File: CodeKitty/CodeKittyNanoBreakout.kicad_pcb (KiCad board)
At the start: 2 copper layers, 17.8 x 43.2 mm, 11 parts, among them P1 CONN_01X02, P2 CONN_01X02, P3 CONN_01X03, P4 CONN_01X03, P5 CONN_01X02, U1 ArduinoNano

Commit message: update of codekitty
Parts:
- removed R3: R, Resistors_SMD:R_0805_HandSoldering
- added F1: F_Small, DM_Custom:DM_FUSE_PTC0ZCG, B.Cu at (201.5, 93.7)
- added SP1: SPEAKER, DM_Custom:DM_PiezSMD_PMKCS0909E4000-R1, B.Cu at (205.6, 114.3)
- added SW1: SW_PUSH_SMALL_H, DM_Custom:DM_SMD_BUTTON_PTS810, F.Cu at (203.7, 84.3)
- added SW2: Switch_SPDT_x2, DM_Custom:DM_SPDT_RTAngle_JS102011SAQN, B.Cu at (203.8, 84.5)
- R1: moved to F.Cu
- U1: moved to B.Cu
- moved G*** 25.0 mm to (205.4, 111.2)
- moved R2 20.3 mm to (209.5, 87.3), turned to 90 degrees
- moved P4 13.2 mm to (209.5, 105.7), turned to 0 degrees
- moved P2 10.5 mm to (205.6, 94.5), turned to 0 degrees
- moved R1 10.2 mm to (209.5, 87.3)
- moved P5 9.86 mm to (201.7, 105.7), turned to 0 degrees
- moved P3 6.37 mm to (205.7, 105.7), turned to 0 degrees
- moved D1 5.35 mm to (210.9, 83.7), turned to 180 degrees
- moved P1 4.17 mm to (209.6, 94.5), turned to 0 degrees
- moved U1 0.06 mm to (205.7, 104.1)
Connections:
- P1 pad 2: VCC -> Net-(P1-Pad2)
- P5 pad 2: Net-(P5-Pad2) -> BUZZ
- U1 pad 3: Net-(U1-Pad3) -> RST
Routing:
- net RST: track 0.00 -> 40.5 mm, vias 0 -> 2
- net GND: track 4.40 -> 26.9 mm, vias 0 -> 3
- net TAIL: track 24.4 -> 3.95 mm, vias 1 -> 0
- net VCC: track 12.0 -> 32.1 mm, vias 1 -> 2
- net 5V: track 52.5 -> 37.6 mm, vias 1 -> 0
- net RSERVO: track 5.23 -> 15.2 mm
- net BUZZ: track 22.5 -> 32.1 mm
- net Net-(P1-Pad2): track 0.00 -> 8.56 mm, vias 0 -> 1
- net Net-(F1-Pad1): track 0.00 -> 7.31 mm
- net Net-(D1-Pad1): track 9.52 -> 4.48 mm, vias 0 -> 1
- net LSERVO: track 5.50 -> 10.4 mm
- net Net-(P2-Pad2): track 3.88 -> 8.13 mm, vias 0 -> 2
- net Net-(P5-Pad2): track 4.04 -> 0.00 mm
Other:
- board text added: "CodeKitty DM100917"
- board text removed: "CodeKitty DM073117"

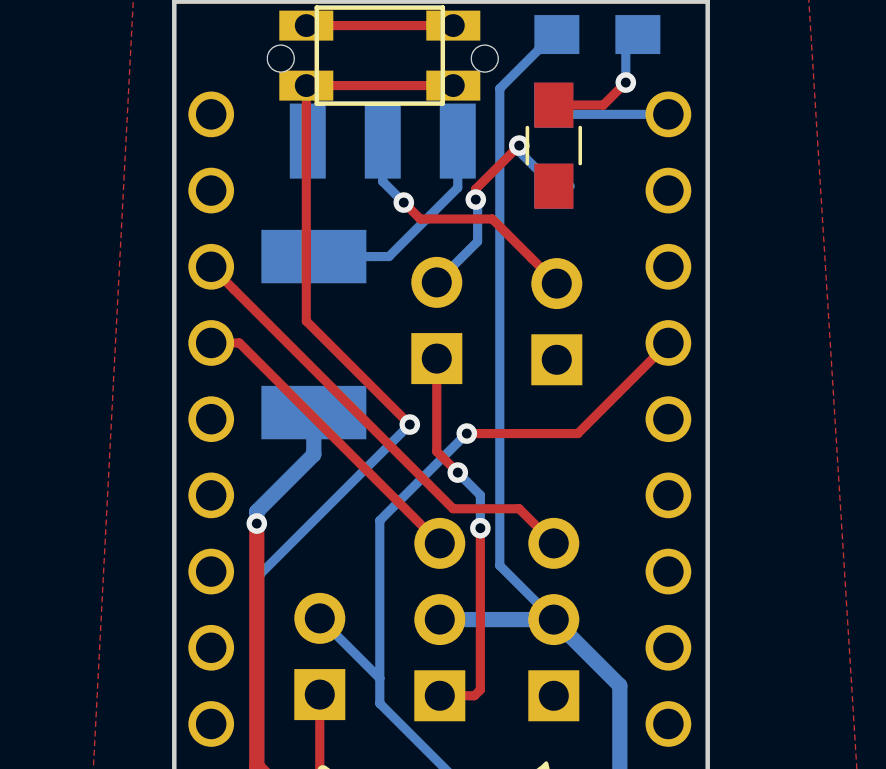
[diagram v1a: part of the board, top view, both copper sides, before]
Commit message: added fsilk letters for connectors for codeKitty
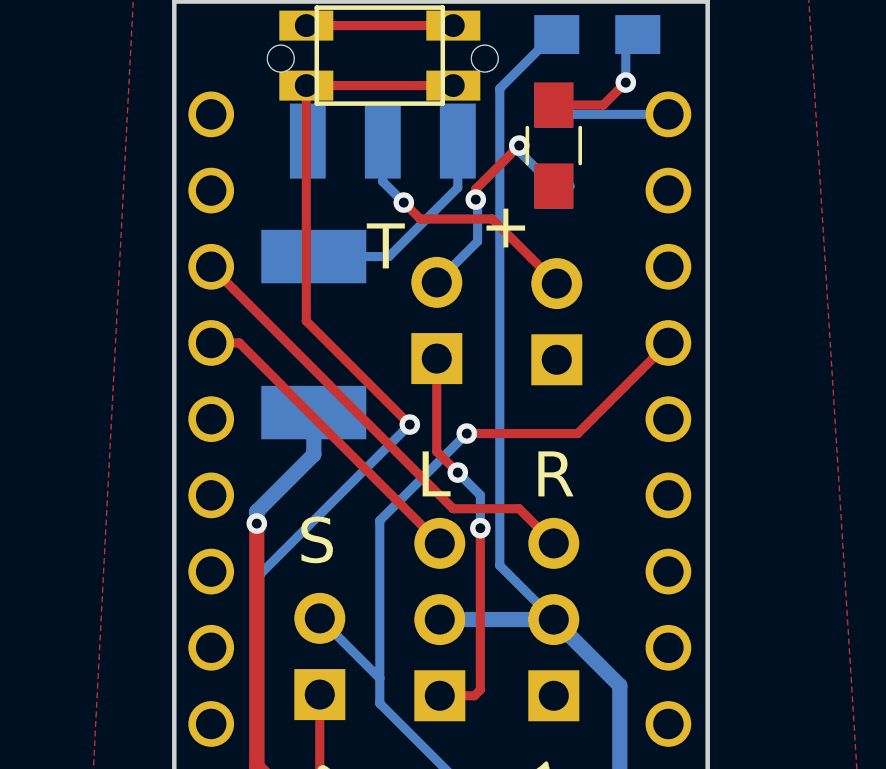
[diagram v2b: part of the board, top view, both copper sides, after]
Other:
- board text added: "+"
- board text added: "L"
- board text added: "R"
- board text added: "S"
- board text added: "T"
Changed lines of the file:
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@@
     (area 196.774999 82.474999 214.705001 125.805001)
     (thickness 1.6)
-    (drawings 16)
+    (drawings 21)
     (tracks 83)
     (zones 0)
@@
     (0 F.Cu signal)
     (31 B.Cu signal)
-    (32 B.Adhes user hide)
-    (33 F.Adhes user hide)
-    (34 B.Paste user hide)
-    (35 F.Paste user hide)
-    (36 B.SilkS user hide)
-    (37 F.SilkS user hide)
-    (38 B.Mask user hide)
+    (32 B.Adhes user)
+    (33 F.Adhes user)
+    (34 B.Paste user)
+    (35 F.Paste user)
+    (36 B.SilkS user)
+    (37 F.SilkS user)
+    (38 B.Mask user)
     (39 F.Mask user)
     (40 Dwgs.User user hide)
@@
     (42 Eco1.User user hide)
     (43 Eco2.User user hide)
-    (44 Edge.Cuts user hide)
+    (44 Edge.Cuts user)
     (45 Margin user hide)
     (46 B.CrtYd user hide)
@@
     (pad "" np_thru_hole circle (at 3.4 0) (size 0.9 0.9) (drill 0.9) (layers *.Cu *.Mask))
   )
+  (gr_text S (at 201.6 100.55) (layer F.SilkS)
+    (effects (font (size 1.5 1.5) (thickness 0.3)))
+  )
+  (gr_text L (at 205.5 98.35) (layer F.SilkS)
+    (effects (font (size 1.5 1.5) (thickness 0.3)))
+  )
+  (gr_text R (at 209.5 98.35) (layer F.SilkS)
+    (effects (font (size 1.5 1.5) (thickness 0.3)))
+  )
+  (gr_text T (at 203.9 90.75) (layer F.SilkS)
+    (effects (font (size 1.5 1.5) (thickness 0.3)))
+  )
+  (gr_text + (at 207.9 90.05) (layer F.SilkS)
+    (effects (font (size 1.5 1.5) (thickness 0.3)))
+  )
   (gr_text 1 (at 186.1 78.55) (layer B.SilkS)

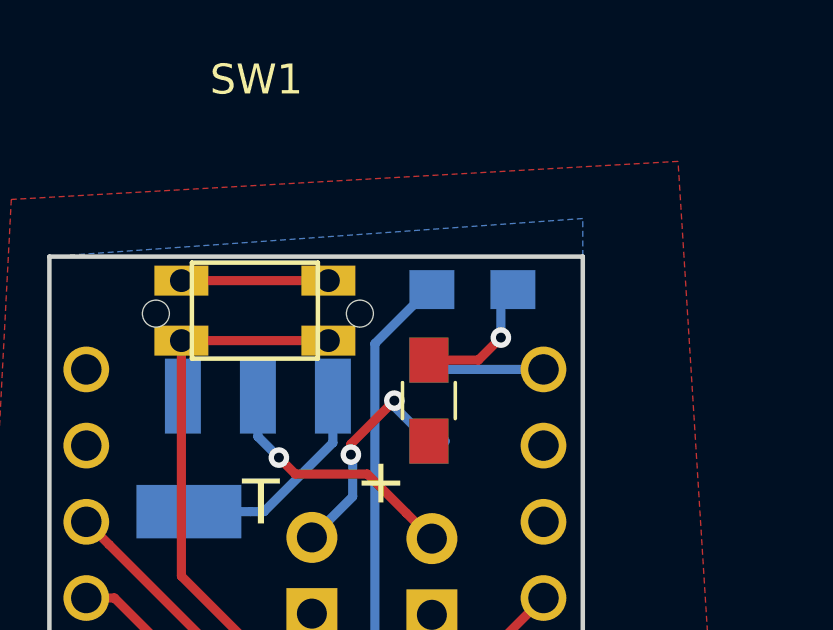
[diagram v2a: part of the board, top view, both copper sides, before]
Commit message: moved led to fside ck
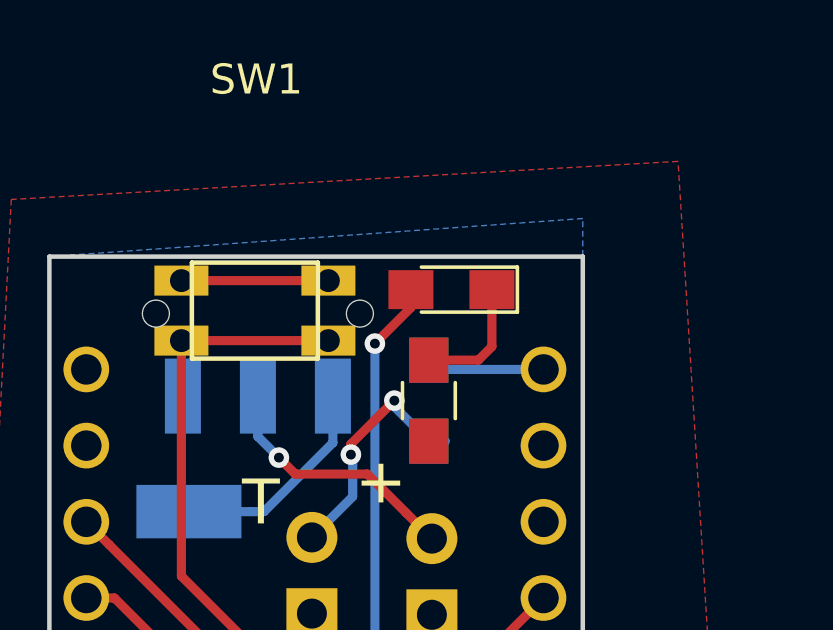
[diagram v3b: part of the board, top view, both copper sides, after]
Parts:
- D1: moved to F.Cu
- moved D1 0.70 mm to (210.2, 83.7)
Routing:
- net 5V: track 37.6 -> 37.2 mm, vias 0 -> 1
- net Net-(D1-Pad1): track 4.48 -> 4.19 mm, vias 1 -> 0
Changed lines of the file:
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@@
     (thickness 1.6)
     (drawings 21)
-    (tracks 83)
+    (tracks 82)
     (zones 0)
     (modules 14)
@@
     (add_net VCC)
   )
-  (module LEDs:LED_0805_HandSoldering (layer B.Cu)
-    (at 210.95 83.65 180)
+  (module LEDs:LED_0805_HandSoldering (layer F.Cu)
+    (at 210.25 83.65 180)
     (descr "Resistor SMD 0805, hand soldering")
     (tags "resistor 0805")
     (attr smd)
-    (fp_text reference D1 (at 0 1.7 180) (layer B.Fab)
-      (effects (font (size 1 1) (thickness 0.15)) (justify mirror))
-    )
-    (fp_text value LED (at 0 -1.75 180) (layer B.Fab)
-      (effects (font (size 1 1) (thickness 0.15)) (justify mirror))
-    )
-    (fp_line (start -0.4 0.4) (end -0.4 -0.4) (layer B.Fab) (width 0.1))
-    (fp_line (start -0.4 0) (end 0.2 0.4) (layer B.Fab) (width 0.1))
-    (fp_line (start 0.2 -0.4) (end -0.4 0) (layer B.Fab) (width 0.1))
-    (fp_line (start 0.2 0.4) (end 0.2 -0.4) (layer B.Fab) (width 0.1))
-    (fp_line (start -1 -0.62) (end -1 0.62) (layer B.Fab) (width 0.1))
-    (fp_line (start 1 -0.62) (end -1 -0.62) (layer B.Fab) (width 0.1))
-    (fp_line (start 1 0.62) (end 1 -0.62) (layer B.Fab) (width 0.1))
-    (fp_line (start -1 0.62) (end 1 0.62) (layer B.Fab) (width 0.1))
-    (fp_line (start 1 -0.75) (end -2.2 -0.75) (layer B.SilkS) (width 0.12))
-    (fp_line (start -2.2 0.75) (end 1 0.75) (layer B.SilkS) (width 0.12))
-    (fp_line (start -2.35 0.9) (end 2.35 0.9) (layer B.CrtYd) (width 0.05))
-    (fp_line (start -2.35 0.9) (end -2.35 -0.9) (layer B.CrtYd) (width 0.05))
-    (fp_line (start 2.35 -0.9) (end 2.35 0.9) (layer B.CrtYd) (width 0.05))
-    (fp_line (start 2.35 -0.9) (end -2.35 -0.9) (layer B.CrtYd) (width 0.05))
-    (fp_line (start -2.2 0.75) (end -2.2 -0.75) (layer B.SilkS) (width 0.12))
-    (pad 1 smd rect (at -1.35 0 180) (size 1.5 1.3) (layers B.Cu B.Paste B.Mask)
+    (fp_text reference D1 (at 0 -1.7 180) (layer F.Fab)
+      (effects (font (size 1 1) (thickness 0.15)))
+    )
+    (fp_text value LED (at 0 1.75 180) (layer F.Fab)
+      (effects (font (size 1 1) (thickness 0.15)))
+    )
+    (fp_line (start -0.4 -0.4) (end -0.4 0.4) (layer F.Fab) (width 0.1))
+    (fp_line (start -0.4 0) (end 0.2 -0.4) (layer F.Fab) (width 0.1))
+    (fp_line (start 0.2 0.4) (end -0.4 0) (layer F.Fab) (width 0.1))
+    (fp_line (start 0.2 -0.4) (end 0.2 0.4) (layer F.Fab) (width 0.1))
+    (fp_line (start -1 0.62) (end -1 -0.62) (layer F.Fab) (width 0.1))
+    (fp_line (start 1 0.62) (end -1 0.62) (layer F.Fab) (width 0.1))
+    (fp_line (start 1 -0.62) (end 1 0.62) (layer F.Fab) (width 0.1))
+    (fp_line (start -1 -0.62) (end 1 -0.62) (layer F.Fab) (width 0.1))
+    (fp_line (start 1 0.75) (end -2.2 0.75) (layer F.SilkS) (width 0.12))
+    (fp_line (start -2.2 -0.75) (end 1 -0.75) (layer F.SilkS) (width 0.12))
+    (fp_line (start -2.35 -0.9) (end 2.35 -0.9) (layer F.CrtYd) (width 0.05))
+    (fp_line (start -2.35 -0.9) (end -2.35 0.9) (layer F.CrtYd) (width 0.05))
+    (fp_line (start 2.35 0.9) (end 2.35 -0.9) (layer F.CrtYd) (width 0.05))
+    (fp_line (start 2.35 0.9) (end -2.35 0.9) (layer F.CrtYd) (width 0.05))
+    (fp_line (start -2.2 -0.75) (end -2.2 0.75) (layer F.SilkS) (width 0.12))
+    (pad 1 smd rect (at -1.35 0 180) (size 1.5 1.3) (layers F.Cu F.Paste F.Mask)
       (net 1 "Net-(D1-Pad1)"))
-    (pad 2 smd rect (at 1.35 0 180) (size 1.5 1.3) (layers B.Cu B.Paste B.Mask)
+    (pad 2 smd rect (at 1.35 0 180) (size 1.5 1.3) (layers F.Cu F.Paste F.Mask)
       (net 2 5V))
     (model ${KISYS3DMOD}/LEDs.3dshapes/LED_0805.wrl
@@
   (gr_line (start 214.63 82.55) (end 214.63 125.73) (layer Edge.Cuts) (width 0.15))
   (gr_line (start 196.85 82.55) (end 214.63 82.55) (layer Edge.Cuts) (width 0.15))
-  (segment (start 211.9 85.25) (end 211.9 84.05) (width 0.3048) (layer B.Cu) (net 1))
-  (segment (start 211.9 84.05) (end 212.3 83.65) (width 0.3048) (layer B.Cu) (net 1))
+  (segment (start 211.15 86) (end 211.6 85.55) (width 0.3048) (layer F.Cu) (net 1))
+  (segment (start 211.6 85.55) (end 211.6 83.65) (width 0.3048) (layer F.Cu) (net 1))
   (segment (start 209.5 86) (end 211.15 86) (width 0.3048) (layer F.Cu) (net 1))
-  (segment (start 211.15 86) (end 211.9 85.25) (width 0.3048) (layer F.Cu) (net 1))
-  (via (at 211.9 85.25) (size 0.6858) (drill 0.3302) (layers F.Cu B.Cu) (net 1))
+  (segment (start 208.9 83.65) (end 208.9 84.25) (width 0.3048) (layer F.Cu) (net 2))
+  (segment (start 208.9 84.25) (end 207.7 85.45) (width 0.3048) (layer F.Cu) (net 2))
+  (via (at 207.7 85.45) (size 0.6858) (drill 0.3302) (layers F.Cu B.Cu) (net 2))
   (segment (start 205.7 103.15) (end 209.5 103.15) (width 0.508) (layer B.Cu) (net 2))
   (segment (start 211.7 105.35) (end 209.5 103.15) (width 0.508) (layer B.Cu) (net 2))
@@
   (segment (start 207.7 85.45) (end 207.7 101.35) (width 0.3048) (layer B.Cu) (net 2))
   (segment (start 207.7 101.35) (end 209.5 103.15) (width 0.3048) (layer B.Cu) (net 2))
-  (segment (start 209.6 83.65) (end 209.5 83.65) (width 0.3048) (layer B.Cu) (net 2))
-  (segment (start 209.5 83.65) (end 207.7 85.45) (width 0.3048) (layer B.Cu) (net 2))
   (segment (start 206.3 98.25) (end 205.6 97.55) (width 0.3048) (layer F.Cu) (net 3))
   (segment (start 205.6 97.55) (end 205.6 94.45) (width 0.3048) (layer F.Cu) (net 3))
